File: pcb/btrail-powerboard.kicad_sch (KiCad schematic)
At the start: 10 parts, among them J1 RJ45_Shielded, Q1 BC328, Q2 BC328, U2 XL1509-5.0

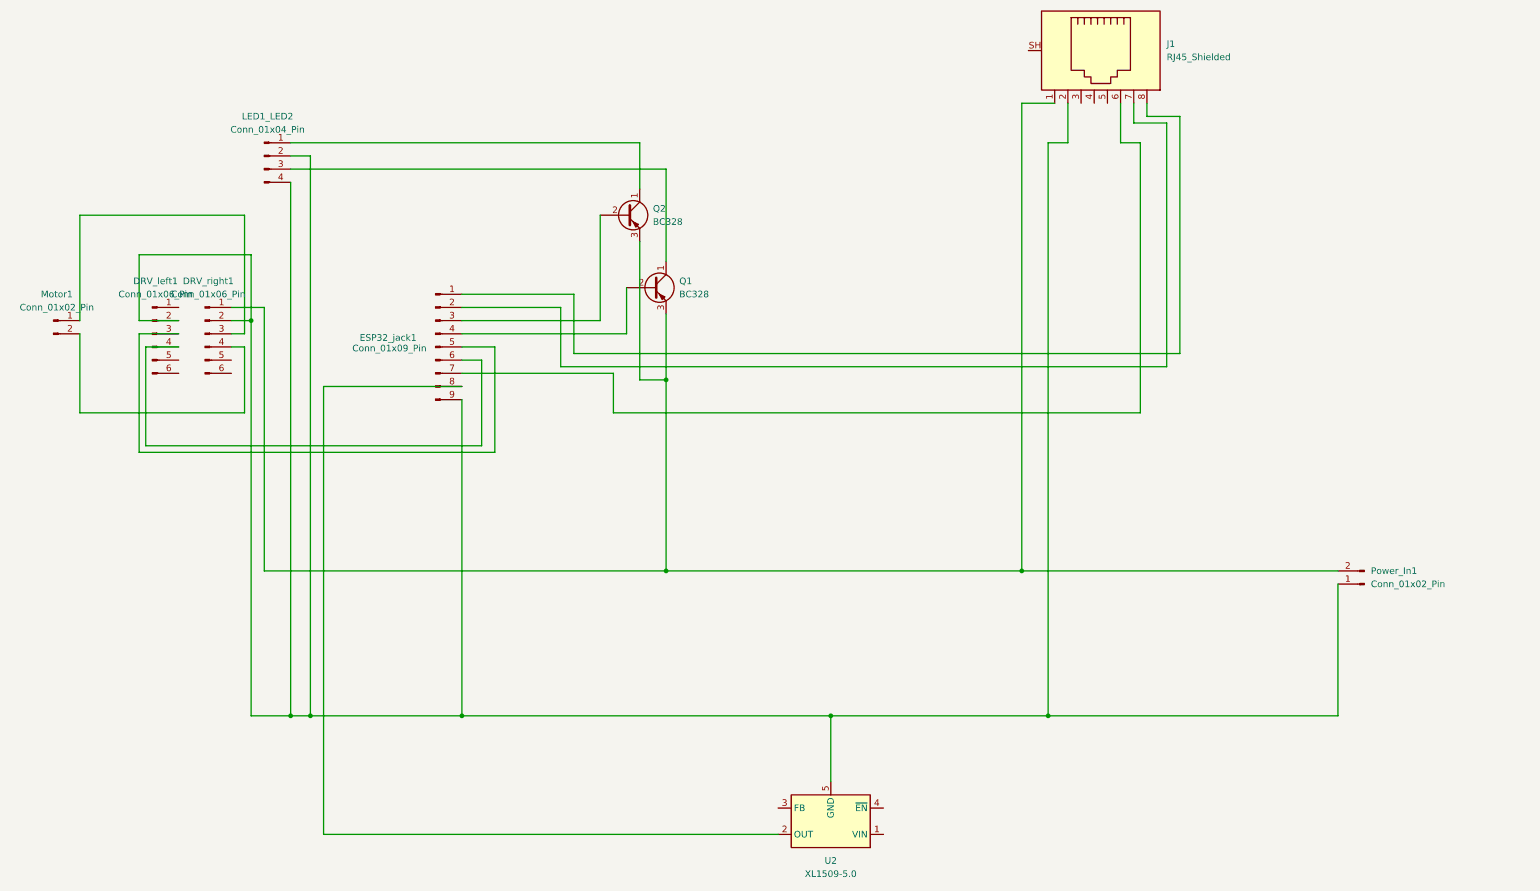
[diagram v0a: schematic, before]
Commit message: Update pcb with symmetrical pin layout on RJ45 jack
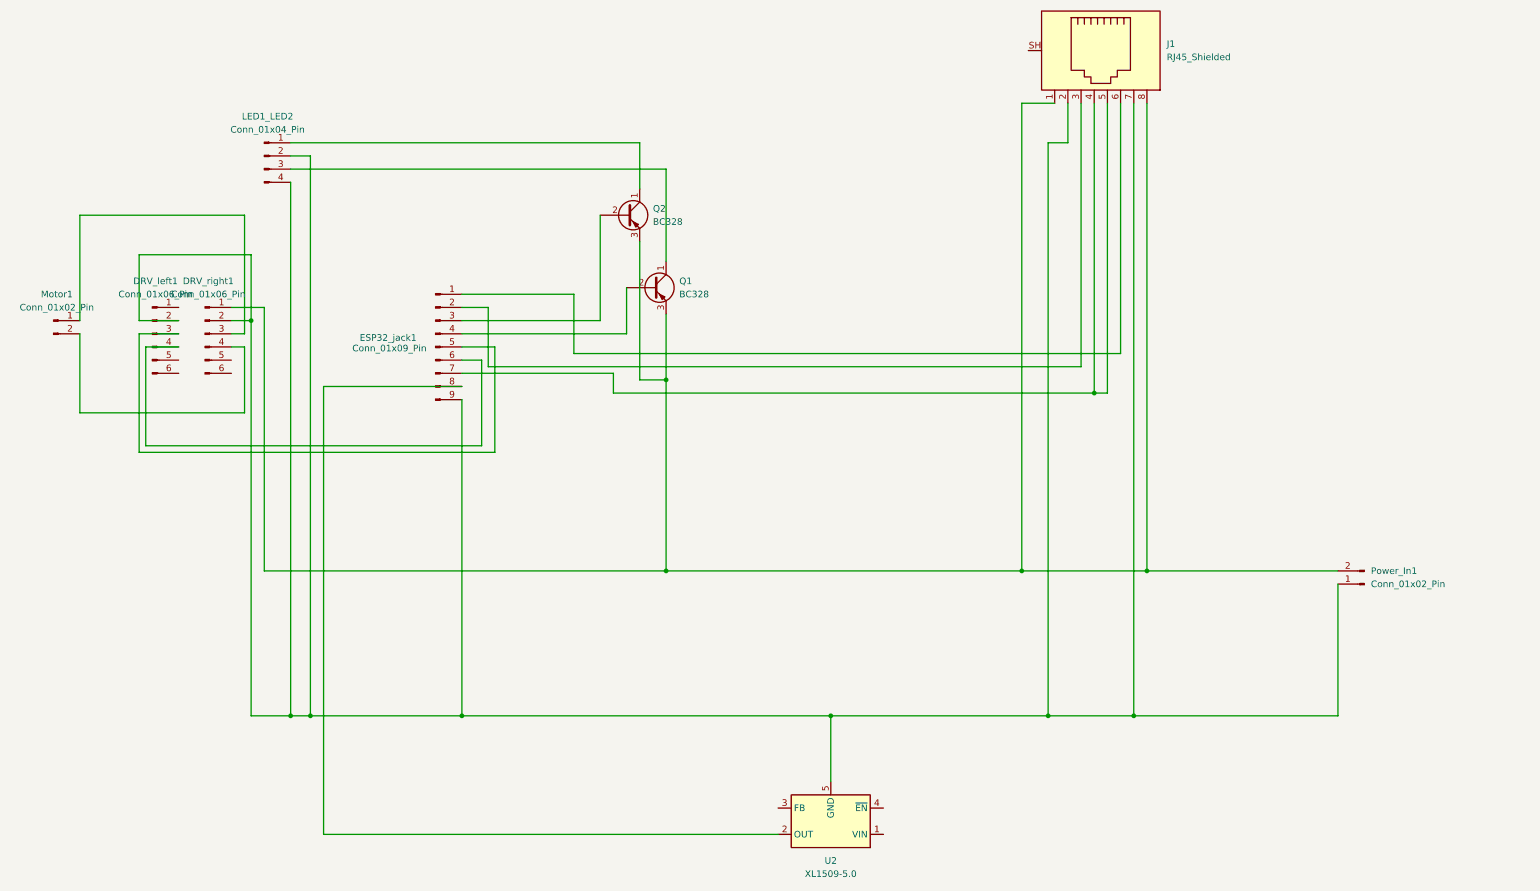
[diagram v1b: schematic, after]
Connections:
- net at DRV_right1.1 (Pin_1), J1.1, Power_In1.2 (Pin_2)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: now also J1.8
- net at DRV_left1.2 (Pin_2), DRV_right1.2 (Pin_2), ESP32_jack1.9 (Pin_9)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: now also J1.7
- net at ESP32_jack1.1 (Pin_1): now also J1.6; no longer J1.8
- net at ESP32_jack1.2 (Pin_2): now also J1.3; no longer J1.7
- net at ESP32_jack1.7 (Pin_7): now also J1.4, J1.5; no longer J1.6
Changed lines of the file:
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@@
+	)
+	(junction
+		(at 214.63 96.52)
+		(diameter 0)
+		(color 0 0 0 0)
 	)
 	(junction
@@
 	)
 	(junction
+		(at 222.25 158.75)
+		(diameter 0)
+		(color 0 0 0 0)
+	)
+	(junction
 		(at 132.08 130.81)
 		(diameter 0)
 		(color 0 0 0 0)
 	)
+	(junction
+		(at 224.79 130.81)
+		(diameter 0)
+		(color 0 0 0 0)
+	)
+	(wire
+		(pts
+			(xy 214.63 96.52) (xy 217.17 96.52)
+		)
+		(stroke
+			(width 0)
+			(type default)
+		)
+	)
 	(wire
 		(pts
@@
 	(wire
 		(pts
-			(xy 228.6 44.45) (xy 222.25 44.45)
-		)
-		(stroke
-			(width 0)
-			(type default)
-		)
-	)
-	(wire
-		(pts
 			(xy 19.05 85.09) (xy 19.05 100.33)
 		)
@@
 	(wire
 		(pts
+			(xy 217.17 40.64) (xy 217.17 96.52)
+		)
+		(stroke
+			(width 0)
+			(type default)
+		)
+	)
+	(wire
+		(pts
 			(xy 200.66 40.64) (xy 207.01 40.64)
 		)
@@
 	(wire
 		(pts
+			(xy 222.25 158.75) (xy 261.62 158.75)
+		)
+		(stroke
+			(width 0)
+			(type default)
+			(color 0 0 0 1)
+		)
+	)
+	(wire
+		(pts
 			(xy 50.8 100.33) (xy 50.8 87.63)
 		)
@@
 	(wire
 		(pts
-			(xy 223.52 48.26) (xy 219.71 48.26)
-		)
-		(stroke
-			(width 0)
-			(type default)
-		)
-	)
-	(wire
-		(pts
 			(xy 163.83 171.45) (xy 163.83 158.75)
 		)
@@
 	(wire
 		(pts
-			(xy 231.14 43.18) (xy 224.79 43.18)
-		)
-		(stroke
-			(width 0)
-			(type default)
-		)
-	)
-	(wire
-		(pts
 			(xy 132.08 53.34) (xy 59.69 53.34)
 		)
@@
 	(wire
 		(pts
-			(xy 111.76 80.01) (xy 92.71 80.01)
+			(xy 97.79 80.01) (xy 92.71 80.01)
 		)
 		(stroke
@@
 	(wire
 		(pts
-			(xy 205.74 158.75) (xy 261.62 158.75)
+			(xy 205.74 158.75) (xy 222.25 158.75)
 		)
 		(stroke
@@
 	(wire
 		(pts
-			(xy 228.6 91.44) (xy 111.76 91.44)
-		)
-		(stroke
-			(width 0)
-			(type default)
-		)
-	)
-	(wire
-		(pts
 			(xy 132.08 130.81) (xy 54.61 130.81)
 		)
@@
 	(wire
 		(pts
-			(xy 222.25 44.45) (xy 222.25 40.64)
-		)
-		(stroke
-			(width 0)
-			(type default)
-		)
-	)
-	(wire
-		(pts
 			(xy 54.61 80.01) (xy 48.26 80.01)
 		)
@@
 	(wire
 		(pts
-			(xy 114.3 88.9) (xy 231.14 88.9)
+			(xy 114.3 88.9) (xy 219.71 88.9)
 		)
 		(stroke
@@
 	(wire
 		(pts
-			(xy 223.52 100.33) (xy 223.52 48.26)
-		)
-		(stroke
-			(width 0)
-			(type default)
-		)
-	)
-	(wire
-		(pts
 			(xy 132.08 130.81) (xy 200.66 130.81)
 		)
@@
 	(wire
 		(pts
+			(xy 212.09 91.44) (xy 97.79 91.44)
+		)
+		(stroke
+			(width 0)
+			(type default)
+		)
+	)
+	(wire
+		(pts
 			(xy 96.52 90.17) (xy 92.71 90.17)
 		)
@@
 	(wire
 		(pts
-			(xy 121.92 92.71) (xy 121.92 100.33)
-		)
-		(stroke
-			(width 0)
-			(type default)
+			(xy 121.92 92.71) (xy 121.92 96.52)
+		)
+		(stroke
+			(width 0)
+			(type default)
+		)
+	)
+	(wire
+		(pts
+			(xy 209.55 40.64) (xy 209.55 48.26)
+		)
+		(stroke
+			(width 0)
+			(type default)
+			(color 0 0 0 1)
 		)
 	)
@@
 	(wire
 		(pts
+			(xy 219.71 40.64) (xy 219.71 88.9)
+		)
+		(stroke
+			(width 0)
+			(type default)
+		)
+	)
+	(wire
+		(pts
 			(xy 99.06 107.95) (xy 30.48 107.95)
 		)
@@
 	(wire
 		(pts
+			(xy 212.09 40.64) (xy 212.09 91.44)
+		)
+		(stroke
+			(width 0)
+			(type default)
+		)
+	)
+	(wire
+		(pts
+			(xy 224.79 130.81) (xy 261.62 130.81)
+		)
+		(stroke
+			(width 0)
+			(type default)
+			(color 255 28 0 1)
+		)
+	)
+	(wire
+		(pts
 			(xy 92.71 87.63) (xy 99.06 87.63)
 		)
@@
 	(wire
 		(pts
-			(xy 219.71 48.26) (xy 219.71 40.64)
-		)
-		(stroke
-			(width 0)
-			(type default)
-		)
-	)
-	(wire
-		(pts
-			(xy 209.55 48.26) (xy 209.55 40.64)
-		)
-		(stroke
-			(width 0)
-			(type default)
-			(color 0 0 0 1)
-		)
-	)
-	(wire
-		(pts
 			(xy 59.69 55.88) (xy 59.69 158.75)
 		)
@@
 	(wire
 		(pts
-			(xy 228.6 44.45) (xy 228.6 91.44)
-		)
-		(stroke
-			(width 0)
-			(type default)
-		)
-	)
-	(wire
-		(pts
-			(xy 231.14 43.18) (xy 231.14 88.9)
-		)
-		(stroke
-			(width 0)
-			(type default)
-		)
-	)
-	(wire
-		(pts
-			(xy 224.79 43.18) (xy 224.79 40.64)
-		)
-		(stroke
-			(width 0)
-			(type default)
-		)
-	)
-	(wire
-		(pts
-			(xy 121.92 100.33) (xy 223.52 100.33)
-		)
-		(stroke
-			(width 0)
-			(type default)
-		)
-	)
-	(wire
-		(pts
-			(xy 200.66 130.81) (xy 261.62 130.81)
+			(xy 222.25 40.64) (xy 222.25 158.75)
+		)
+		(stroke
+			(width 0)
+			(type default)
+			(color 0 0 0 1)
+		)
+	)
+	(wire
+		(pts
+			(xy 121.92 96.52) (xy 214.63 96.52)
+		)
+		(stroke
+			(width 0)
+			(type default)
+		)
+	)
+	(wire
+		(pts
+			(xy 200.66 130.81) (xy 224.79 130.81)
 		)
 		(stroke
@@
 	(wire
 		(pts
+			(xy 214.63 40.64) (xy 214.63 96.52)
+		)
+		(stroke
+			(width 0)
+			(type default)
+		)
+	)
+	(wire
+		(pts
 			(xy 30.48 82.55) (xy 38.1 82.55)
 		)
@@
 	(wire
 		(pts
-			(xy 111.76 91.44) (xy 111.76 80.01)
-		)
-		(stroke
+			(xy 224.79 40.64) (xy 224.79 130.81)
+		)
+		(stroke
+			(width 0)
+			(type default)
+		)
+	)
+	(wire
+		(pts
+			(xy 97.79 91.44) (xy 97.79 80.01)
+		)
+		(stroke

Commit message: Update railBT board with sockets for H-bridge and 5V buck converter
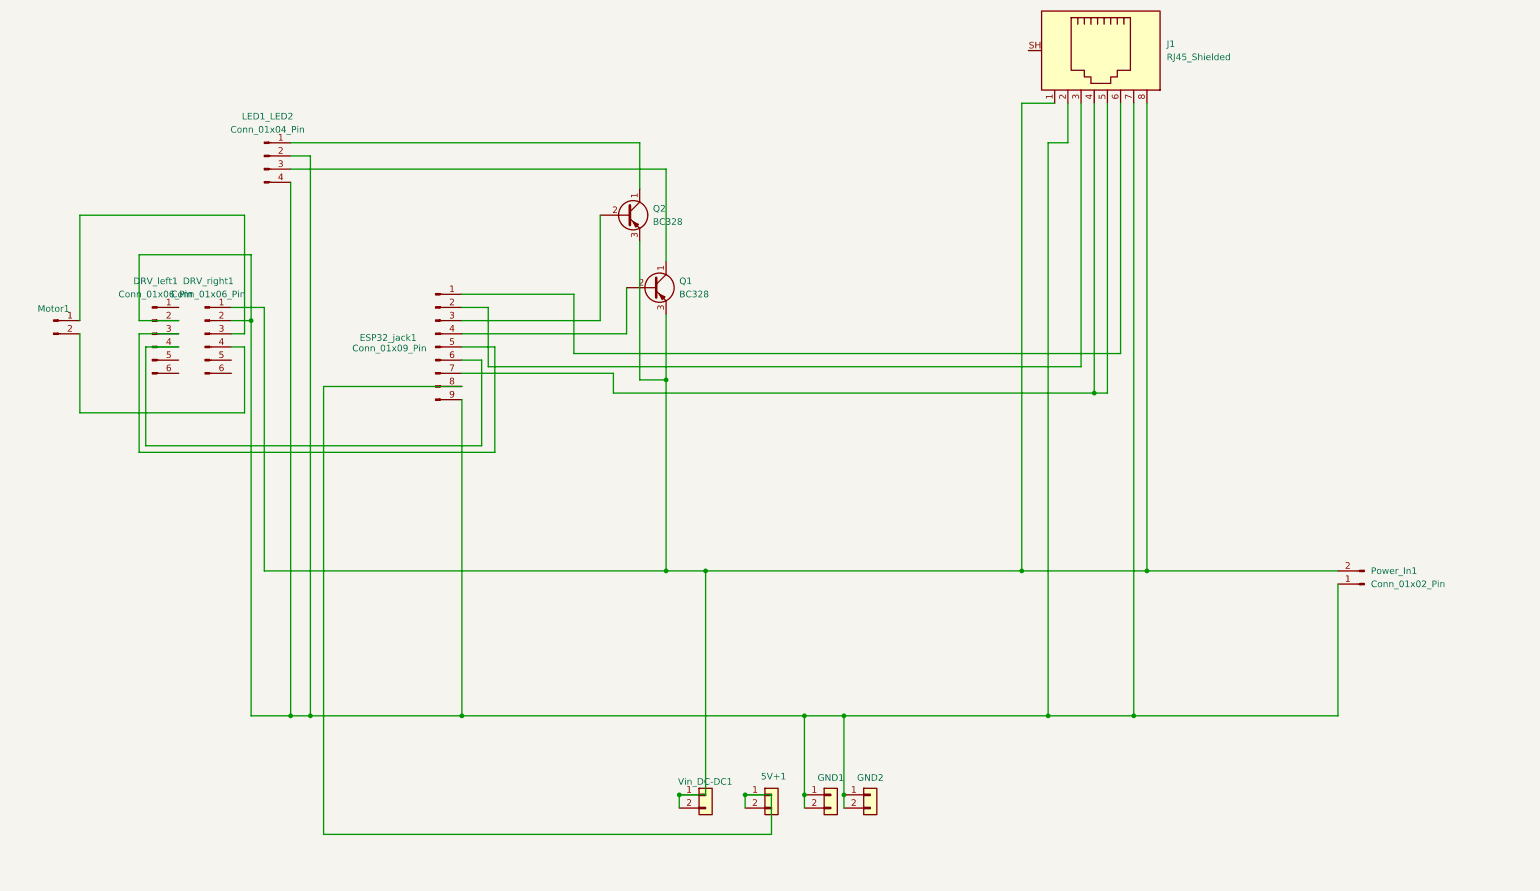
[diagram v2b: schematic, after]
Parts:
- removed U2: XL1509-5.0, Package_SO:SOIC-8_3.9x4.9mm_P1.27mm, symbol Regulator_Switching:XL1509-5.0
- added 5V+1, GND1, GND2: Conn_01x02, Connector_PinSocket_1.00mm:PinSocket_1x02_P1.00mm_Vertical, symbol Connector_Generic:Conn_01x02
- added Vin_DC-DC1: Conn_01x01, Connector_PinSocket_1.00mm:PinSocket_1x02_P1.00mm_Vertical, symbol Connector_Generic:Conn_01x02
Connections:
- net at DRV_right1.1 (Pin_1), J1.1, J1.8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: now also Vin_DC-DC1.1 (Pin_1), Vin_DC-DC1.2 (Pin_2)
- net at DRV_left1.2 (Pin_2), DRV_right1.2 (Pin_2), ESP32_jack1.9 (Pin_9)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: now also GND1.1 (Pin_1), GND1.2 (Pin_2), GND2.1 (Pin_1), GND2.2 (Pin_2)
- net at ESP32_jack1.8 (Pin_8): now also 5V+1.1 (Pin_1), 5V+1.2 (Pin_2)

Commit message: Update PCB to latest revision
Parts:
- removed Q2: BC328, Package_TO_SOT_THT:TO-92_Inline, symbol Transistor_BJT:BC328
- added Q2: IRLZ34N, Package_TO_SOT_THT:TO-220-3_Vertical, symbol Transistor_FET:IRLZ34N
- Q1: value BC328 -> IRLZ34N; footprint Package_TO_SOT_THT:TO-92_Inline -> Package_TO_SOT_THT:TO-220-3_Vertical; symbol Transistor_BJT:BC328 -> Transistor_FET:IRLZ34N
- renumbered Power_In1 to 24V_In1, DRV_left1 to DRV8874_left1, DRV_right1 to DRV8874_right1, LED1_LED2 to LED1/LED2
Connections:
- net at LED1/LED2.1 (Pin_1): now also Q2.2 (D)
- net at ESP32_jack1.3 (Pin_3): now also Q2.1 (G)
- net at 24V_In1.2 (Pin_2), DRV8874_right1.1 (Pin_1), J1.1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: now also Q2.3 (S)
- net at 24V_In1.1 (Pin_1), DRV8874_left1.2 (Pin_2), DRV8874_right1.2 (Pin_2)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: now also DRV8874_right1.6 (Pin_6)
- net at Q1.1 (G): now also ESP32_jack1.4 (Pin_4); no longer LED1/LED2.3 (Pin_3)
- net at Q1.2 (D): now also LED1/LED2.3 (Pin_3); no longer ESP32_jack1.4 (Pin_4)
- net at DRV8874_left1.5 (Pin_5): now also 5V+1.1 (Pin_1), 5V+1.2 (Pin_2), DRV8874_left1.6 (Pin_6), ESP32_jack1.8 (Pin_8)
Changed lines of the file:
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@@
+	)
+	(junction
+		(at 33.02 92.71)
+		(diameter 0)
+		(color 0 0 0 0)
 	)
 	(junction
@@
 	)
 	(junction
+		(at 52.07 92.71)
+		(diameter 0)
+		(color 0 0 0 0)
+	)
+	(junction
+		(at 66.04 181.61)
+		(diameter 0)
+		(color 0 0 0 0)
+	)
+	(junction
 		(at 166.37 173.99)
 		(diameter 0)
@@
 	(wire
 		(pts
+			(xy 33.02 90.17) (xy 38.1 90.17)
+		)
+		(stroke
+			(width 0)
+			(type default)
+			(color 191 99 0 1)
+		)
+	)
+	(wire
+		(pts
 			(xy 217.17 40.64) (xy 217.17 96.52)
 		)
@@
 	(wire
 		(pts
+			(xy 33.02 92.71) (xy 33.02 90.17)
+		)
+		(stroke
+			(width 0)
+			(type default)
+			(color 191 99 0 1)
+		)
+	)
+	(wire
+		(pts
 			(xy 222.25 158.75) (xy 261.62 158.75)
 		)
@@
 	(wire
 		(pts
+			(xy 52.07 92.71) (xy 52.07 158.75)
+		)
+		(stroke
+			(width 0)
+			(type default)
+			(color 0 0 0 1)
+		)
+	)
+	(wire
+		(pts
 			(xy 38.1 87.63) (xy 31.75 87.63)
 		)
@@
 	(wire
 		(pts
+			(xy 48.26 92.71) (xy 52.07 92.71)
+		)
+		(stroke
+			(width 0)
+			(type default)
+			(color 0 0 0 1)
+		)
+	)
+	(wire
+		(pts
 			(xy 92.71 77.47) (xy 114.3 77.47)
 		)
@@
 	(wire
 		(pts
-			(xy 127 57.15) (xy 127 48.26)
+			(xy 127 48.26) (xy 127 57.15)
 		)
 		(stroke
@@
 	(wire
 		(pts
+			(xy 33.02 181.61) (xy 33.02 92.71)
+		)
+		(stroke
+			(width 0)
+			(type default)
+			(color 191 99 0 1)
+		)
+	)
+	(wire
+		(pts
 			(xy 96.52 90.17) (xy 92.71 90.17)
 		)
@@
 	(wire
 		(pts
+			(xy 66.04 181.61) (xy 33.02 181.61)
+		)
+		(stroke
+			(width 0)
+			(type default)
+			(color 191 99 0 1)
+		)
+	)
+	(wire
+		(pts
 			(xy 92.71 158.75) (xy 158.75 158.75)
 		)
@@
 	(wire
 		(pts
-			(xy 52.07 82.55) (xy 52.07 158.75)
+			(xy 52.07 82.55) (xy 52.07 92.71)
 		)
 		(stroke
@@
 	(wire
 		(pts
+			(xy 33.02 92.71) (xy 38.1 92.71)
+		)
+		(stroke
+			(width 0)
+			(type default)
+			(color 191 99 0 1)
+		)
+	)
+	(wire
+		(pts
 			(xy 166.37 173.99) (xy 166.37 176.53)
 		)
@@
 			(type default)
 			(color 255 252 0 1)
-		)
-	)
-	(symbol
-		(lib_id "Transistor_BJT:BC328")
-		(at 124.46 62.23 0)
-		(unit 1)
-		(exclude_from_sim no)
-		(in_bom yes)
-		(on_board yes)
-		(dnp no)
-		(fields_autoplaced yes)
-		(property "Reference" "Q2"
-			(at 129.54 60.9599 0)
-			(effects
-				(font
-					(size 1.27 1.27)
-				)
-				(justify left)
-			)
-		)
-		(property "Value" "BC328"
-			(at 129.54 63.4999 0)
-			(effects
-				(font
-					(size 1.27 1.27)
-				)
-				(justify left)
-			)
-		)
-		(property "Footprint" "Package_TO_SOT_THT:TO-92_Inline"
-			(at 129.54 64.135 0)
-			(effects
-				(font
-					(size 1.27 1.27)
-					(italic yes)
-				)
-				(justify left)
-				(hide yes)
-			)
-		)
-		(property "Datasheet" "http://www.redrok.com/PNP_BC327_-45V_-800mA_0.625W_Hfe100_TO-92.pdf"
-			(at 124.46 62.23 0)
-			(effects
-				(font
-					(size 1.27 1.27)
-				)
-				(justify left)
-				(hide yes)
-			)
-		)
-		(property "Description" "0.8A Ic, 25V Vce, PNP Transistor, TO-92"
-			(at 124.46 62.23 0)
-			(effects
-				(font
-					(size 1.27 1.27)
-				)
-				(hide yes)
-			)
-		)
-		(pin "1"
-		)
-		(pin "2"
-		)
-		(pin "3"
-		)
-		(instances
-			(project ""
-				(path "/fc5fcd3d-9ac1-47d3-89b1-872aad02a51d"
-					(reference "Q2")
-					(unit 1)
-				)
-			)
 		)
 	)
@@
 		(dnp no)
 		(fields_autoplaced yes)
-		(property "Reference" "DRV_right1"
+		(property "Reference" "DRV8874_right1"
 			(at 43.815 74.93 0)
 			(effects
@@
 			(project ""
 				(path "/fc5fcd3d-9ac1-47d3-89b1-872aad02a51d"
-					(reference "DRV_right1")
+					(reference "DRV8874_right1")
 					(unit 1)
 				)
@@
 	)
 	(symbol
-		(lib_id "Transistor_BJT:BC328")
+		(lib_id "Transistor_FET:IRLZ34N")
 		(at 129.54 76.2 0)
 		(unit 1)
@@
 		(fields_autoplaced yes)
 		(property "Reference" "Q1"
-			(at 134.62 74.9299 0)
+			(at 135.89 74.9299 0)
 			(effects
 				(font
@@
 			)
 		)
-		(property "Value" "BC328"
-			(at 134.62 77.4699 0)
+		(property "Value" "IRLZ34N"
+			(at 135.89 77.4699 0)
 			(effects
 				(font
@@
 			)
 		)
-		(property "Footprint" "Package_TO_SOT_THT:TO-92_Inline"
+		(property "Footprint" "Package_TO_SOT_THT:TO-220-3_Vertical"
 			(at 134.62 78.105 0)
 			(effects
@@
 			)
 		)
-		(property "Datasheet" "http://www.redrok.com/PNP_BC327_-45V_-800mA_0.625W_Hfe100_TO-92.pdf"
-			(at 129.54 76.2 0)
+		(property "Datasheet" "https://www.infineon.com/dgdl/irf1324pbf.pdf?fileId=5546d462533600a4015355dac93318a7"
+			(at 134.62 80.01 0)
 			(effects
 				(font
@@
 			)
 		)
-		(property "Description" "0.8A Ic, 25V Vce, PNP Transistor, TO-92"
+		(property "Description" "INFINEON MOSFET, N-Ch 24V 195A 0,0012R, TO-220"
 			(at 129.54 76.2 0)
 			(effects
@@
 		(dnp no)
 		(fields_autoplaced yes)
-		(property "Reference" "Power_In1"
+		(property "Reference" "24V_In1"
 			(at 267.97 130.8099 0)
 			(effects
@@
 			(project ""
 				(path "/fc5fcd3d-9ac1-47d3-89b1-872aad02a51d"
-					(reference "Power_In1")
+					(reference "24V_In1")
 					(unit 1)
 				)
@@
 		(dnp no)
 		(fields_autoplaced yes)
-		(property "Reference" "DRV_left1"
+		(property "Reference" "DRV8874_left1"
 			(at 33.655 74.93 0)
 			(effects
@@
 			(project ""
 				(path "/fc5fcd3d-9ac1-47d3-89b1-872aad02a51d"
-					(reference "DRV_left1")
+					(reference "DRV8874_left1")
 					(unit 1)
 				)
@@
 		(dnp no)
 		(fields_autoplaced yes)
-		(property "Reference" "LED1_LED2"
+		(property "Reference" "LED1/LED2"
 			(at 55.245 43.18 0)
 			(effects
@@
 			(project ""
 				(path "/fc5fcd3d-9ac1-47d3-89b1-872aad02a51d"
-					(reference "LED1_LED2")
+					(reference "LED1/LED2")
 					(unit 1)
 				)
@@
 					(unit 1)
 				)
+			)
+		)
+	)
+	(symbol
+		(lib_id "Transistor_FET:IRLZ34N")
+		(at 124.46 62.23 0)
+		(unit 1)
+		(exclude_from_sim no)
+		(in_bom yes)
+		(on_board yes)
+		(dnp no)
+		(fields_autoplaced yes)
+		(property "Reference" "Q2"
+			(at 130.81 60.9599 0)
+			(effects
+				(font
+					(size 1.27 1.27)
+				)
+				(justify left)
+			)
+		)
+		(property "Value" "IRLZ34N"
+			(at 130.81 63.4999 0)
+			(effects
+				(font
+					(size 1.27 1.27)
+				)
+				(justify left)
+			)
+		)
+		(property "Footprint" "Package_TO_SOT_THT:TO-220-3_Vertical"
+			(at 129.54 64.135 0)
+			(effects
+				(font
+					(size 1.27 1.27)
+					(italic yes)
+				)
+				(justify left)
+				(hide yes)
+			)
+		)
+		(property "Datasheet" "https://www.infineon.com/dgdl/irf1324pbf.pdf?fileId=5546d462533600a4015355dac93318a7"
+			(at 129.54 66.04 0)
+			(effects
+				(font
+					(size 1.27 1.27)
+				)
+				(justify left)
+				(hide yes)
+			)
+		)
+		(property "Description" "INFINEON MOSFET, N-Ch 24V 195A 0,0012R, TO-220"
+			(at 124.46 62.23 0)
+			(effects
+				(font
+					(size 1.27 1.27)
+				)
+				(hide yes)
+			)
+		)
+		(pin "2"
+		)
+		(pin "1"
+		)
+		(pin "3"
+		)
+		(instances
+			(project "btrail-powerboard"
+				(path "/fc5fcd3d-9ac1-47d3-89b1-872aad02a51d"
+					(reference "Q2")
+					(unit 1)
+				)
